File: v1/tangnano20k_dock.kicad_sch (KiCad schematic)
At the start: 42 parts, among them J1 Mini-DIN-6, J2 2x20 Pin Female, J3 Conn_01x03_Male, J4 Conn_01x20, J5 Conn_01x02, J6 RCA, J7 FCR684205T, J8 AudioJack3, U1 TXS0104E, U2 TangNano20K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

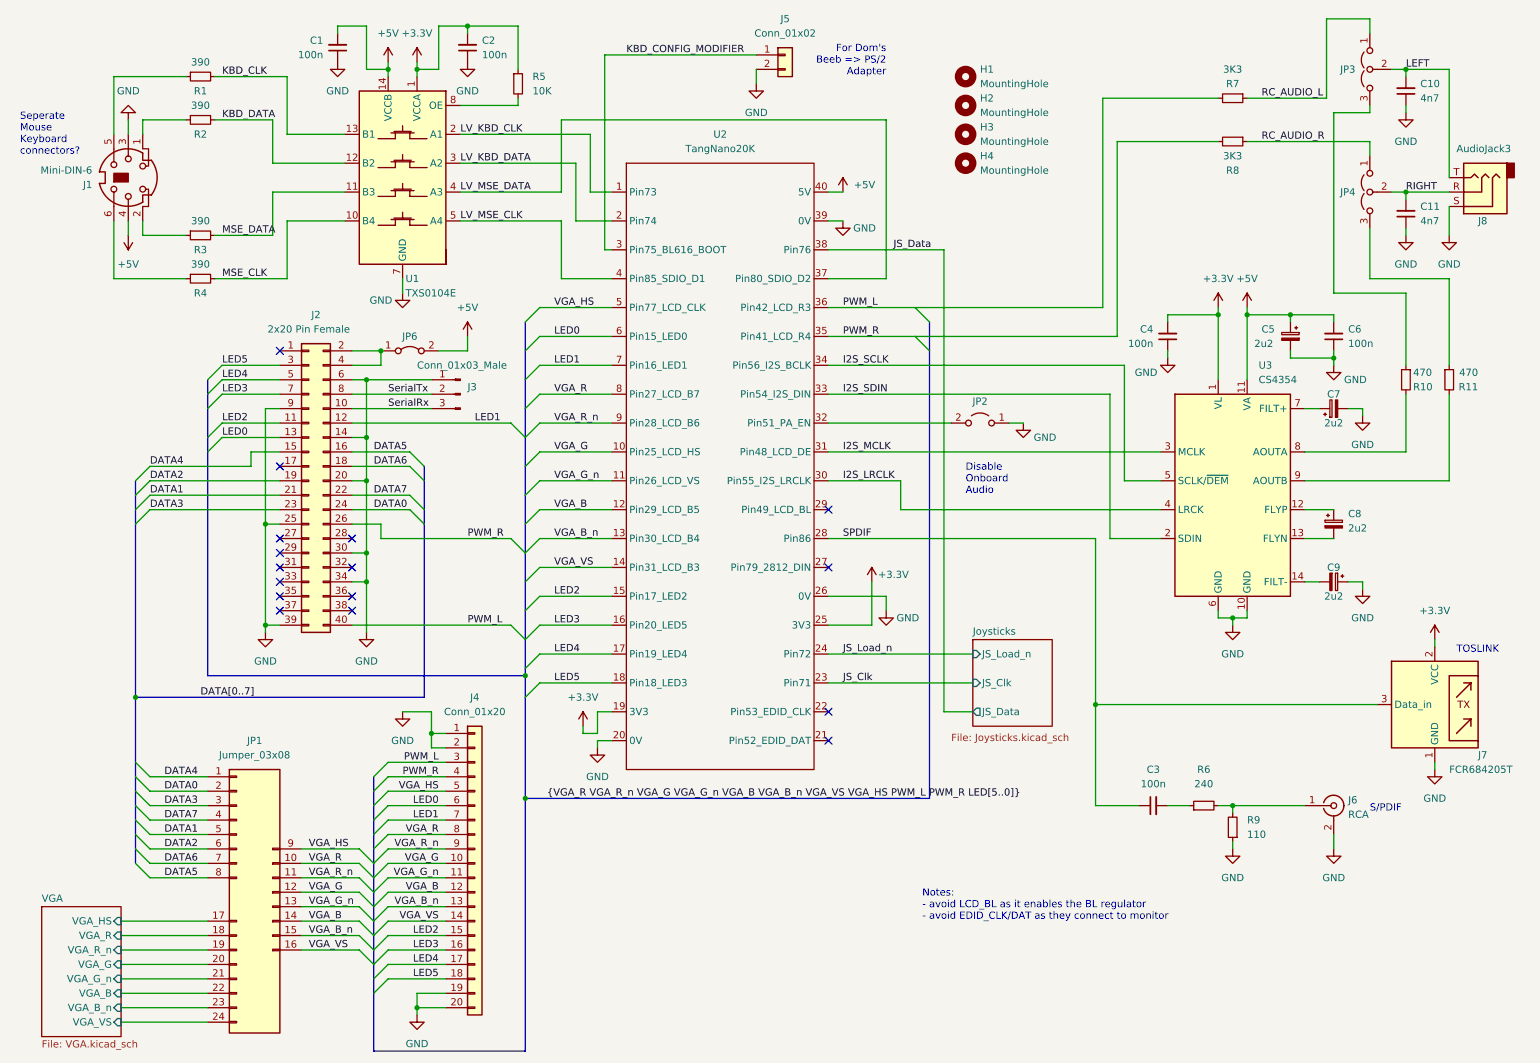
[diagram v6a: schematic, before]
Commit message: Drive PiTube PHI2 from WS2812 output, freeing up PWM
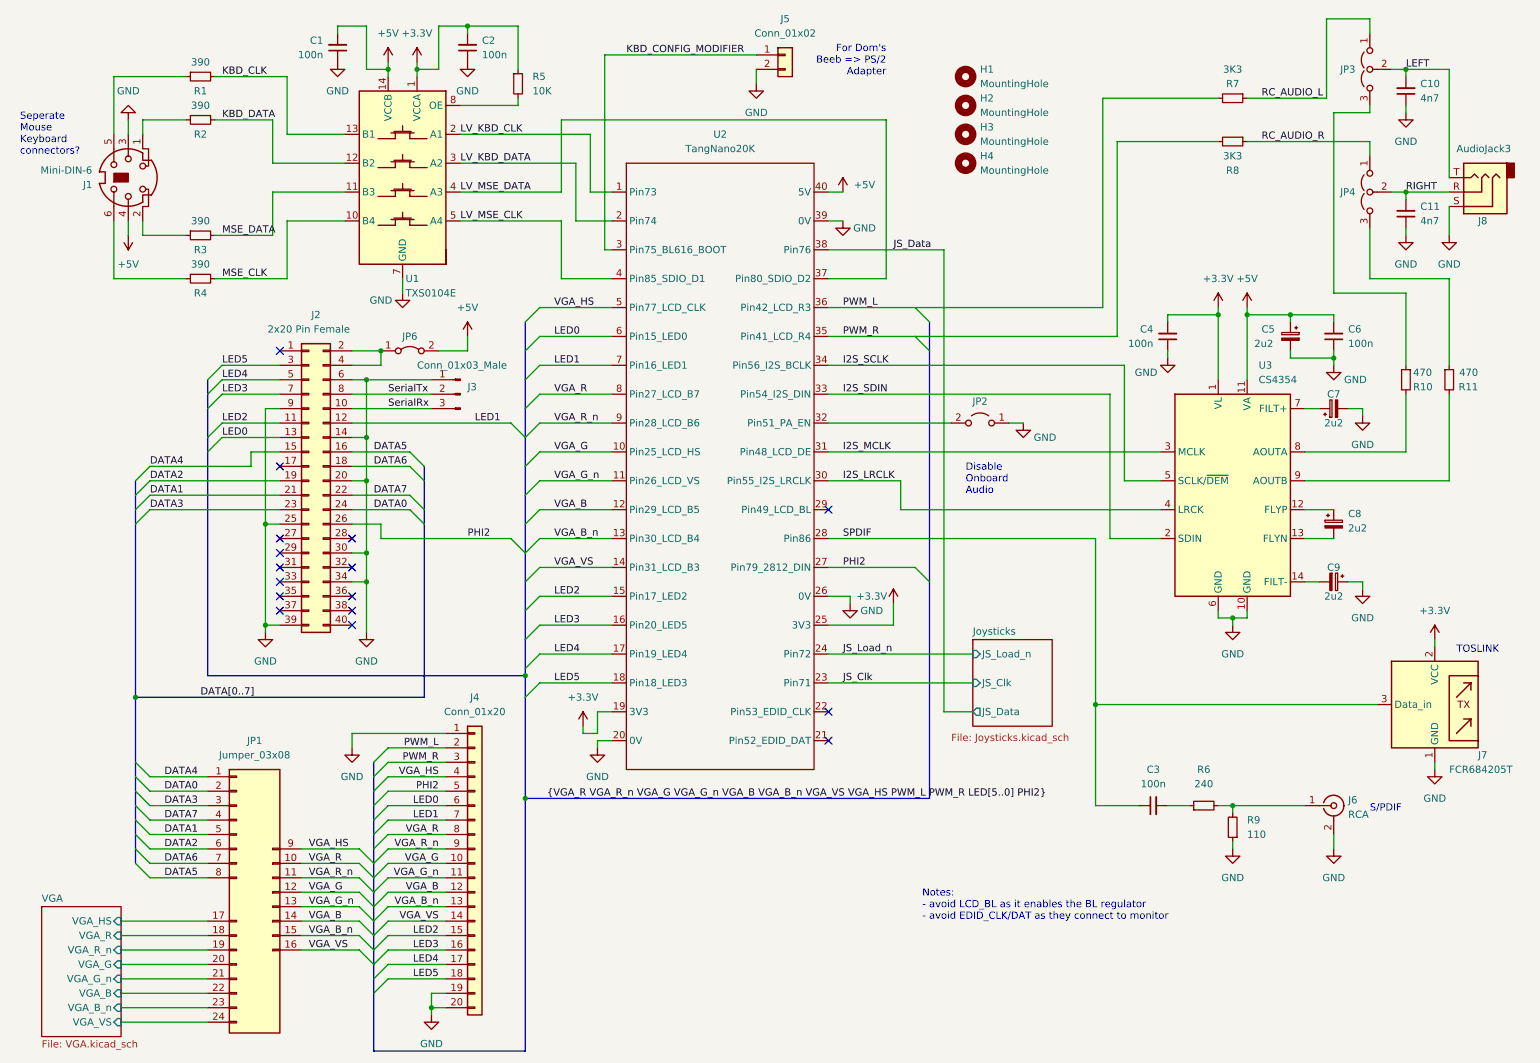
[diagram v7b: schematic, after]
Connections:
- net GND: no longer J4.2 (Pin_2)
- net PWM_L: now also J4.2 (Pin_2); no longer J2.40 (Pin_40), J4.3 (Pin_3)
- net PWM_R: now also J4.3 (Pin_3); no longer J2.26 (Pin_26), J4.4 (Pin_4)
- net VGA_HS: now also J4.4 (Pin_4); no longer J4.5 (Pin_5)
- net PHI2: now reaches U2.27 (Pin79_2812_DIN)
- net PHI2: now also J2.26 (Pin_26), J4.5 (Pin_5)

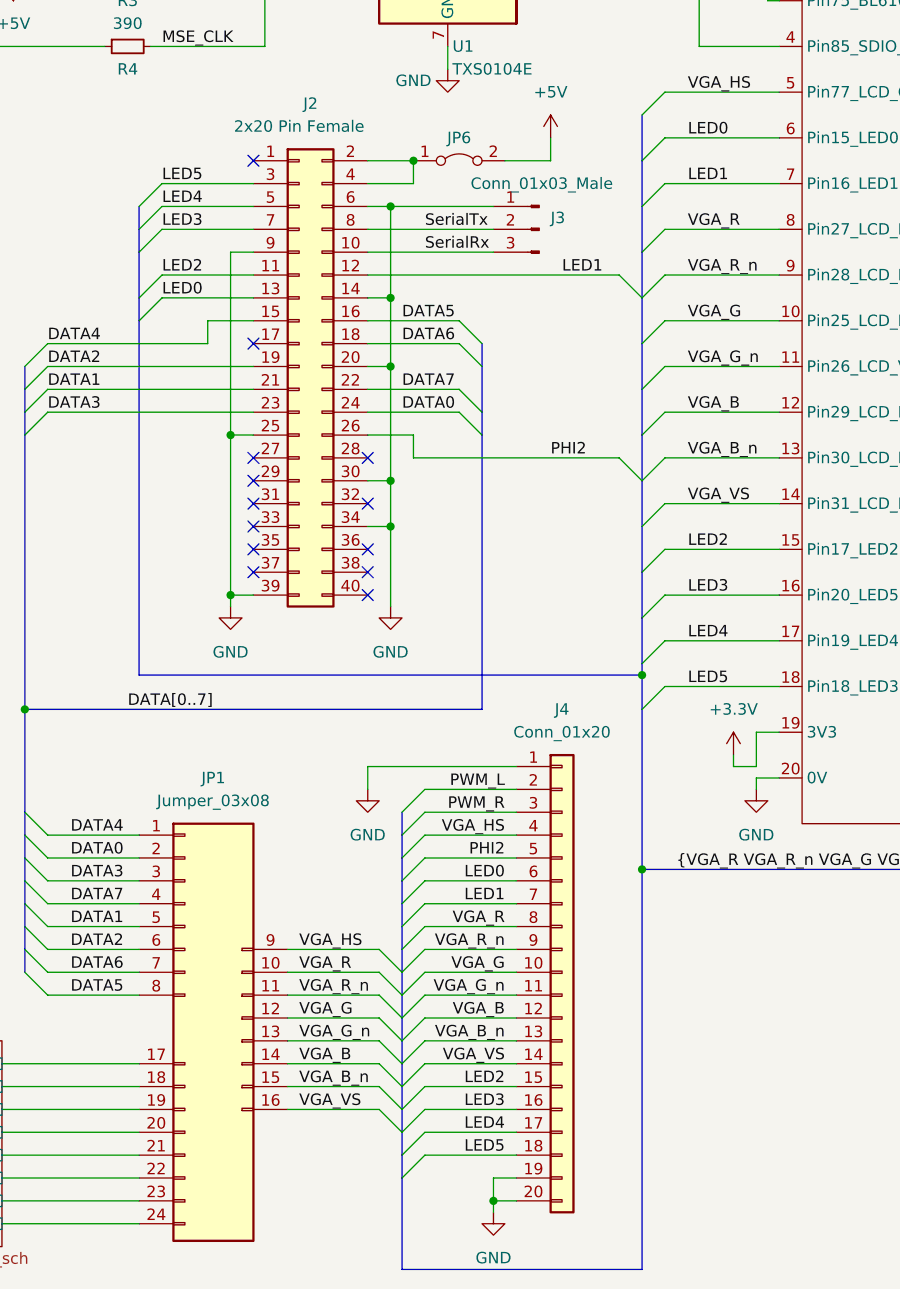
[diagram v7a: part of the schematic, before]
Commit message: Correct swapped net names LED3 and LED5
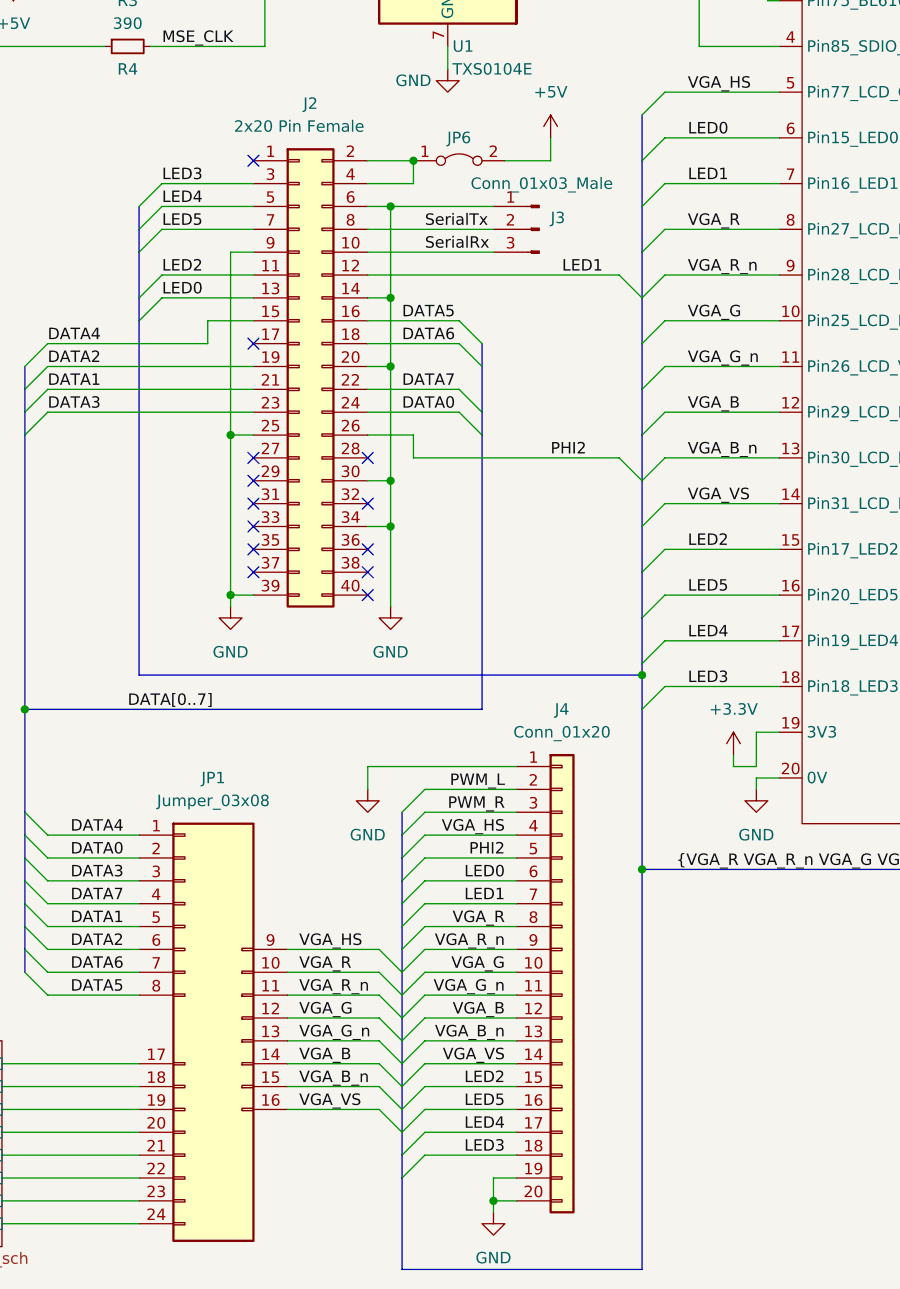
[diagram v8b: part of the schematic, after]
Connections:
- net LED3: now also J2.3 (Pin_3), J4.18 (Pin_18), U2.18 (Pin18_LED3); no longer J2.7 (Pin_7), J4.16 (Pin_16), U2.16 (Pin20_LED5)
- net LED5: now also J2.7 (Pin_7), J4.16 (Pin_16), U2.16 (Pin20_LED5); no longer J2.3 (Pin_3), J4.18 (Pin_18), U2.18 (Pin18_LED3)
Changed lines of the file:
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@@
     (effects (font (size 1.27 1.27)) (justify left bottom))
   )
-  (label "LED3" (at 113.03 120.65 0)
+  (label "LED5" (at 113.03 120.65 0)
     (effects (font (size 1.27 1.27)) (justify left bottom))
   )
@@
     (effects (font (size 1.27 1.27)) (justify left bottom))
   )
-  (label "LED5" (at 92.71 182.88 180)
+  (label "LED3" (at 92.71 182.88 180)
     (effects (font (size 1.27 1.27)) (justify right bottom))
   )
@@
     (effects (font (size 1.27 1.27)) (justify right bottom))
   )
-  (label "LED5" (at 54.61 74.93 0)
+  (label "LED3" (at 54.61 74.93 0)
     (effects (font (size 1.27 1.27)) (justify left bottom))
   )
@@
     (effects (font (size 1.27 1.27)) (justify left bottom))
   )
-  (label "LED3" (at 54.61 80.01 0)
+  (label "LED5" (at 54.61 80.01 0)
     (effects (font (size 1.27 1.27)) (justify left bottom))
   )
@@
     (effects (font (size 1.27 1.27)) (justify left bottom))
   )
-  (label "LED5" (at 113.03 130.81 0)
-    (effects (font (size 1.27 1.27)) (justify left bottom))
-  )
-  (label "LED3" (at 92.71 177.8 180)
-    (effects (font (size 1.27 1.27)) (justify right bottom))
-  )
+  (label "LED3" (at 113.03 130.81 0)
+    (effects (font (size 1.27 1.27)) (justify left bottom))
+  )
+  (label "LED5" (at 92.71 177.8 180)
+    (effects (font (size 1.27 1.27)) (justify right bottom))
+  )
